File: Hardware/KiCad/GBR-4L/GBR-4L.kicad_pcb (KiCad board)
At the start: 4 copper layers, 160 x 100 mm, 188 parts, among them J1 USB4105-GF-A, J101 EM7565 M.2 Key B socket, J102 MODEM_CONTROL, J201 EM7565 M.2 Key B socket, J202 MODEM_CONTROL, J301 EM7565 M.2 Key B socket, J302 MODEM_CONTROL, J401 EM7565 M.2 Key B socket, J402 MODEM_CONTROL, J511 2452808-1 nano-SIM, J521 2452808-1 nano-SIM, J531 2452808-1 nano-SIM, J541 2452808-1 nano-SIM, J701 12V INPUT 5A, Q701 30V P-MOSFET low-RDS(on), Q911 MMBT3906, Q921 MMBT3906, Q931 MMBT3906, Q941 MMBT3906, SW911 MODEM 1 RESET, SW912 MODEM 1 RF DISABLE, SW921 MODEM 2 RESET, SW922 MODEM 2 RF DISABLE, SW931 MODEM 3 RESET, SW932 MODEM 3 RF DISABLE, SW941 MODEM 4 RESET, SW942 MODEM 4 RF DISABLE, U1 USBLC6-2SC6, U11 LOW-CAP SIM ESD ARRAY, U12 LOW-CAP SIM ESD ARRAY, U13 LOW-CAP SIM ESD ARRAY, U14 LOW-CAP SIM ESD ARRAY, U2 USB2514Bi-I/M2, U21 TPS56339DDCR, U22 TPS56339DDCR, U23 TPS56339DDCR, U24 TPS56339DDCR, U25 TPS56339DDCR, Y1 24MHz

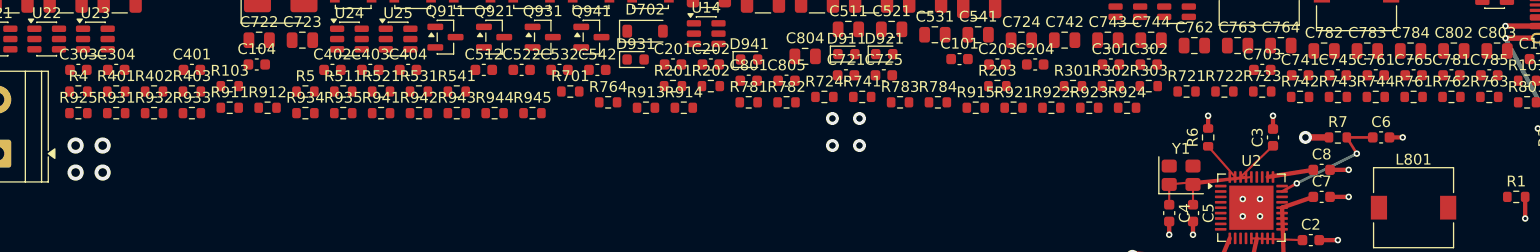
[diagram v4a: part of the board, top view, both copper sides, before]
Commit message: Place and route USB VBUS detect divider
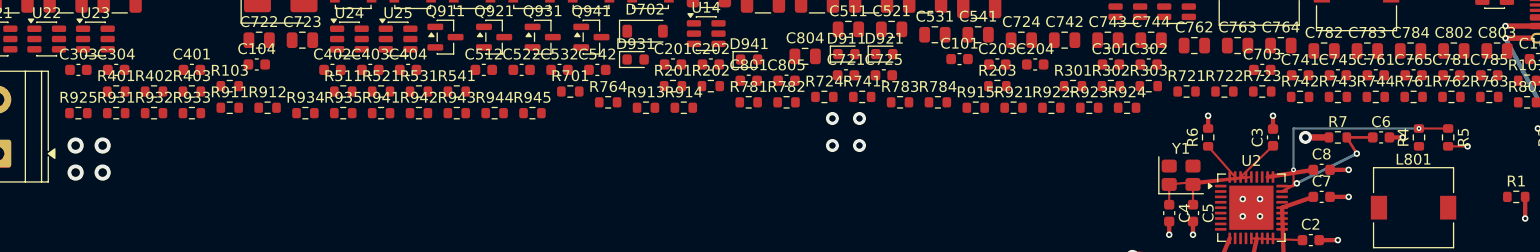
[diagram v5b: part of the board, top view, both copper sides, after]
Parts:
- moved R4 124.1 mm to (160.5, 48.5), turned to 90 degrees
- moved R5 105.8 mm to (163.2, 48.5), turned to -90 degrees
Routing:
- net USB_VBUS_DET: track 0.00 -> 20.7 mm, vias 0 -> 2
- net GND: track 30.3 -> 32.1 mm, vias 66 -> 67
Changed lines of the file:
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@@
 	(footprint "Resistor_SMD:R_0603_1608Metric"
 		(layer "F.Cu")
-		(at 57.505 44.255)
+		(at 163.2 48.5 -90)
 		(descr "Resistor SMD 0603 (1608 Metric), square (rectangular) end terminal, IPC-7351 nominal, (Body size source: IPC-SM-782 page 72, https://www.pcb-3d.com/wordpress/wp-content/uploads/ipc-sm-782a_amendment_1_and_2.pdf)")
 		(tags "resistor")
 		(property "Reference" "R5"
-			(at 0 -1.43 0)
+			(at 0 -1.43 270)
 			(layer "F.SilkS")
 			(effects
@@
 		)
 		(property "Value" "100k 1%"
-			(at 0 1.43 0)
+			(at 0 1.43 270)
 			(layer "F.Fab")
 			(effects
@@
 		)
 		(property "Datasheet" ""
-			(at 0 0 0)
+			(at 0 0 270)
 			(layer "F.Fab")
 			(hide yes)
@@
 		)
 		(property "Description" ""
-			(at 0 0 0)
+			(at 0 0 270)
 			(layer "F.Fab")
 			(hide yes)
@@
 		)
 		(property "KiLib_Generator" "SMD_2terminal_chip_molded"
-			(at 0 0 0)
+			(at 0 0 270)
 			(layer "F.SilkS")
 			(hide yes)
@@
 		(duplicate_pad_numbers_are_jumpers no)
 		(fp_line
-			(start -0.237258 -0.5225)
-			(end 0.237258 -0.5225)
+			(start -0.237258 0.5225)
+			(end 0.237258 0.5225)
 			(stroke
 				(width 0.12)
@@
 		)
 		(fp_line
-			(start -0.237258 0.5225)
-			(end 0.237258 0.5225)
+			(start -0.237258 -0.5225)
+			(end 0.237258 -0.5225)
 			(stroke
 				(width 0.12)
@@
 		)
 		(fp_text user "${REFERENCE}"
-			(at 0 0 0)
+			(at 0 0 270)
 			(layer "F.Fab")
 			(effects
@@
 		)
 		(pad "1" smd roundrect
-			(at -0.825 0)
+			(at -0.825 0 270)
 			(size 0.8 0.95)
 			(layers "F.Cu" "F.Mask" "F.Paste")
@@
 		)
 		(pad "2" smd roundrect
-			(at 0.825 0)
+			(at 0.825 0 270)
 			(size 0.8 0.95)
 			(layers "F.Cu" "F.Mask" "F.Paste")
@@
 	(footprint "Resistor_SMD:R_0603_1608Metric"
 		(layer "F.Cu")
-		(at 36.505 44.254999)
+		(at 160.5 48.5 90)
 		(descr "Resistor SMD 0603 (1608 Metric), square (rectangular) end terminal, IPC-7351 nominal, (Body size source: IPC-SM-782 page 72, https://www.pcb-3d.com/wordpress/wp-content/uploads/ipc-sm-782a_amendment_1_and_2.pdf)")
 		(tags "resistor")
 		(property "Reference" "R4"
-			(at 0 -1.43 0)
+			(at 0 -1.43 90)
 			(layer "F.SilkS")
 			(effects
@@
 		)
 		(property "Value" "100k 1%"
-			(at 0 1.43 0)
+			(at 0 1.43 90)
 			(layer "F.Fab")
 			(effects
@@
 		)
 		(property "Datasheet" ""
-			(at 0 0 0)
+			(at 0 0 90)
 			(layer "F.Fab")
 			(hide yes)
@@
 		)
 		(property "Description" ""
-			(at 0 0 0)
+			(at 0 0 90)
 			(layer "F.Fab")
 			(hide yes)
@@
 		)
 		(property "KiLib_Generator" "SMD_2terminal_chip_molded"
-			(at 0 0 0)
+			(at 0 0 90)
 			(layer "F.SilkS")
 			(hide yes)
@@
 		)
 		(fp_text user "${REFERENCE}"
-			(at 0 0 0)
+			(at 0 0 90)
 			(layer "F.Fab")
 			(effects
@@
 		)
 		(pad "1" smd roundrect
-			(at -0.825 0)
+			(at -0.825 0 90)
 			(size 0.8 0.95)
 			(layers "F.Cu" "F.Mask" "F.Paste")
@@
 		)
 		(pad "2" smd roundrect
-			(at 0.825 0)
+			(at 0.825 0 90)
 			(size 0.8 0.95)
 			(layers "F.Cu" "F.Mask" "F.Paste")
@@
 	)
 	(segment
+		(start 163.2 49.325)
+		(end 165 49.325)
+		(width 0.2)
+		(layer "F.Cu")
+		(net "GND")
+	)
+	(segment
 		(start 145 61.775)
 		(end 145 63)
@@
 	)
 	(via
+		(at 165 49.325)
+		(size 0.6)
+		(drill 0.3)
+		(layers "F.Cu" "B.Cu")
+		(net "GND")
+	)
+	(via
 		(at 45 75)
 		(size 0.6)
@@
 	)
 	(segment
+		(start 147.838 53)
+		(end 148.9 53)
+		(width 0.2)
+		(layer "F.Cu")
+		(net "USB_VBUS_DET")
+	)
+	(segment
+		(start 148.9 53)
+		(end 148.9 51.5)
+		(width 0.2)
+		(layer "F.Cu")
+		(net "USB_VBUS_DET")
+	)
+	(segment
+		(start 160.5 47.675)
+		(end 163.2 47.675)
+		(width 0.2)
+		(layer "F.Cu")
+		(net "USB_VBUS_DET")
+	)
+	(via
+		(at 160.5 47.675)
+		(size 0.45)
+		(drill 0.2)
+		(layers "F.Cu" "B.Cu")
+		(net "USB_VBUS_DET")
+	)
+	(via
+		(at 148.9 51.5)
+		(size 0.45)
+		(drill 0.2)
+		(layers "F.Cu" "B.Cu")
+		(net "USB_VBUS_DET")
+	)
+	(segment
+		(start 148.9 47.675)
+		(end 160.5 47.675)
+		(width 0.2)
+		(layer "B.Cu")
+		(net "USB_VBUS_DET")
+	)
+	(segment
+		(start 148.9 51.5)
+		(end 148.9 47.675)
+		(width 0.2)
+		(layer "B.Cu")
+		(net "USB_VBUS_DET")
+	)
+	(segment

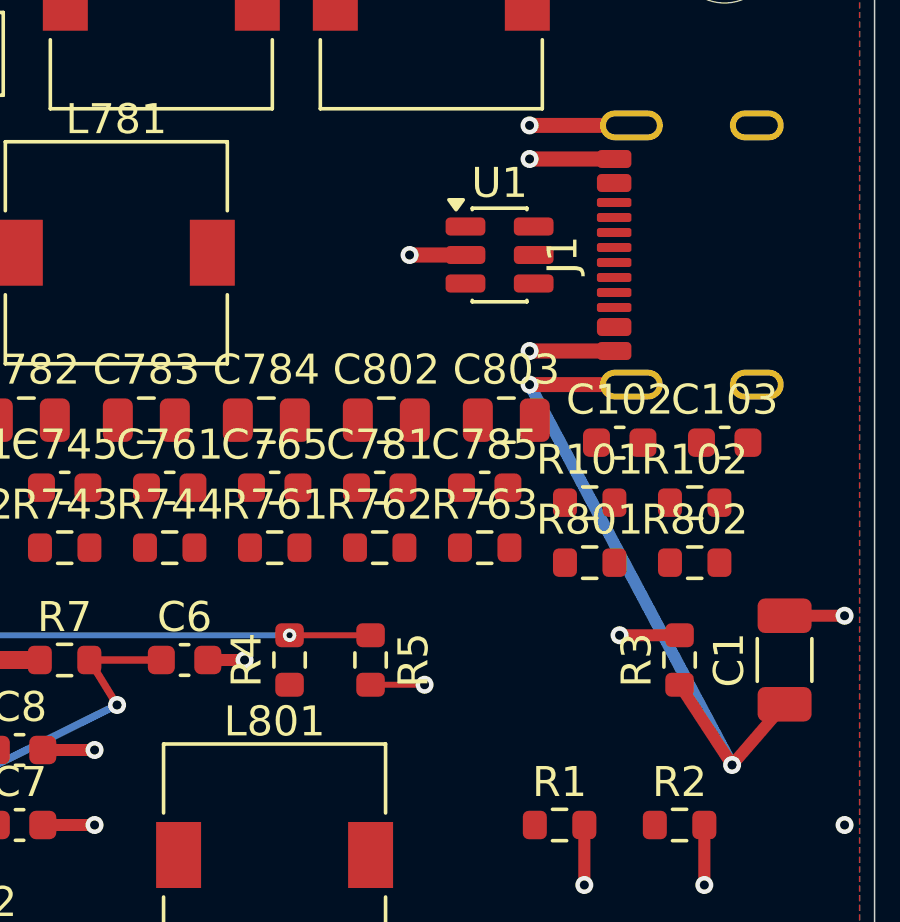
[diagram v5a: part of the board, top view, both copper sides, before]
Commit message: Route USB VBUS entry to detector
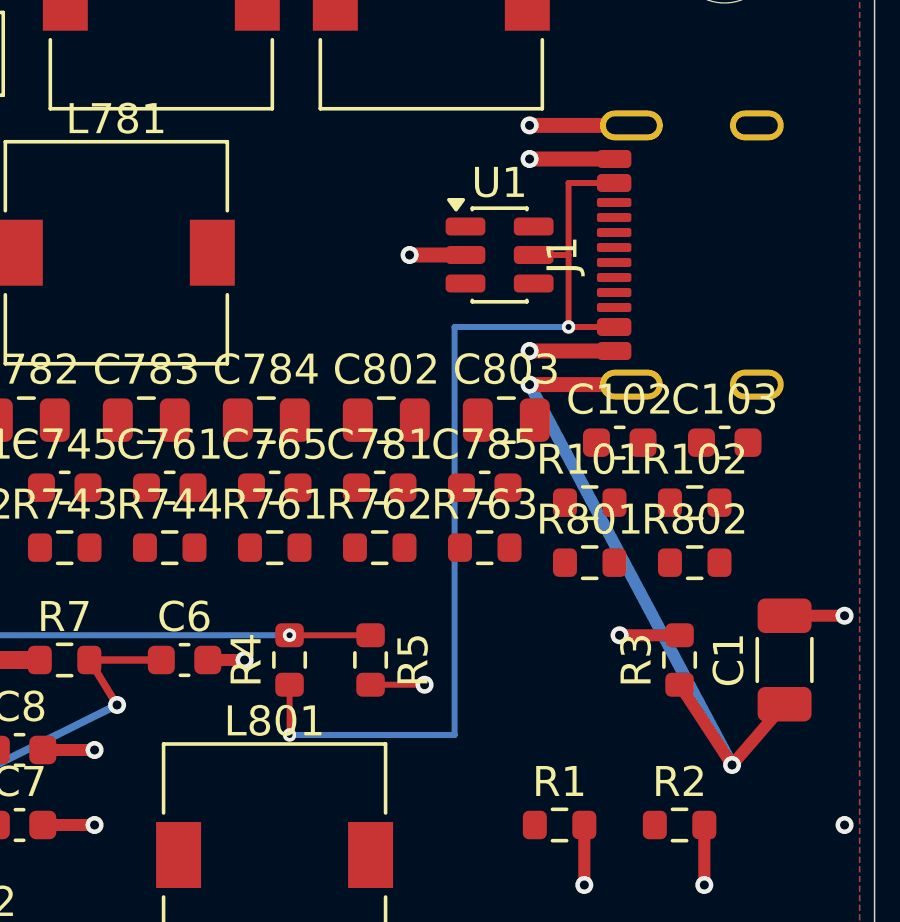
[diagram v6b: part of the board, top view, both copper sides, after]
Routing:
- net USB_VBUS: track 0.00 -> 33.6 mm, vias 0 -> 2
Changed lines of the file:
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@@
+	)
+	(segment
+		(start 171.32 32.6)
+		(end 169.8 32.6)
+		(width 0.2)
+		(layer "F.Cu")
+		(net "USB_VBUS")
+	)
+	(segment
+		(start 160.5 51)
+		(end 160.5 49.325)
+		(width 0.2)
+		(layer "F.Cu")
+		(net "USB_VBUS")
+	)
+	(segment
+		(start 169.8 35)
+		(end 168.637 35)
+		(width 0.2)
+		(layer "F.Cu")
+		(net "USB_VBUS")
+	)
+	(segment
+		(start 171.32 37.4)
+		(end 169.8 37.4)
+		(width 0.2)
+		(layer "F.Cu")
+		(net "USB_VBUS")
+	)
+	(segment
+		(start 169.8 32.6)
+		(end 169.8 37.4)
+		(width 0.2)
+		(layer "F.Cu")
+		(net "USB_VBUS")
+	)
+	(via
+		(at 160.5 51)
+		(size 0.45)
+		(drill 0.2)
+		(layers "F.Cu" "B.Cu")
+		(net "USB_VBUS")
+	)
+	(via
+		(at 169.8 37.4)
+		(size 0.45)
+		(drill 0.2)
+		(layers "F.Cu" "B.Cu")
+		(net "USB_VBUS")
+	)
+	(segment
+		(start 166 37.4)
+		(end 166 51)
+		(width 0.2)
+		(layer "B.Cu")
+		(net "USB_VBUS")
+	)
+	(segment
+		(start 166 51)
+		(end 160.5 51)
+		(width 0.2)
+		(layer "B.Cu")
+		(net "USB_VBUS")
+	)
+	(segment
+		(start 169.8 37.4)
+		(end 166 37.4)
+		(width 0.2)
+		(layer "B.Cu")
+		(net "USB_VBUS")
 	)
 	(segment
